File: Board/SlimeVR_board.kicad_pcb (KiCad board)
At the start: 2 copper layers, 55.8 x 44.5 mm, 44 parts, among them IC1 HT7833, J1 USB_C_Receptacle_USB2.0_16P, J2 Conn_01x02_Pin, J3 Conn_01x04_Pin, J5 Conn_01x01_Pin, J6 Conn_01x01_Pin, J7 Conn_01x04_Pin, Q1 DMP3099L, SW1 SW_SPDT, U1 TP4056-42-ESOP8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

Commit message: New Version
skiped few version that ware bad or not good or not funcioning
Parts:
- removed 3V3, 5V, BAT: TestPoint_Pad_1.5x1.5mm, TestPoint:TestPoint_Pad_1.5x1.5mm
- removed the GND at (82.3, 34.4)
- removed the GND at (47.3, 36.0)
- removed the GND at (43.0, 58.9)
- removed REF** (x2): TestPoint_Pad_D1.0mm, TestPoint:TestPoint_Pad_D1.0mm
- added +3.3V: TestPoint_Pad_1.0x1.0mm, TestPoint:TestPoint_Pad_1.0x1.0mm, F.Cu at (66.6, 39.0)
- added +5V: TestPoint_Pad_1.0x1.0mm, TestPoint:TestPoint_Pad_1.0x1.0mm, F.Cu at (44.0, 40.2)
- added BAT+: TestPoint_Pad_1.0x1.0mm, TestPoint:TestPoint_Pad_1.0x1.0mm, F.Cu at (42.0, 55.2)
- added BMI160 #2 GND: TestPoint_Pad_1.5x1.5mm, TestPoint:TestPoint_Pad_1.5x1.5mm, F.Cu at (48.6, 52.2)
- added GND: TestPoint_Pad_1.0x1.0mm, TestPoint:TestPoint_Pad_1.0x1.0mm, F.Cu at (39.9, 55.2)
- added GND: TestPoint_Pad_1.0x1.0mm, TestPoint:TestPoint_Pad_1.0x1.0mm, F.Cu at (73.8, 27.1)
- D1: value LED -> FYLS-1206URC
- D2: value LED -> FYLS-1206PGC
- D3: value LED -> FYLS-1206UWC
- D4: value D -> 1N4148WSQ-7-F
- J2: value Conn_01x02_Pin -> JST-PH
- J3: value Conn_01x04_Pin -> SMD_Pads; footprint Connector_PinSocket_2.54mm:PinSocket_1x04_P2.54mm_Vertical -> Custom:Pin_1x04_SMD_P2.54mm
- J7: value Conn_01x04_Pin -> JTX-HX
- Q1: value DMP3099L -> DMP3099L-7
- R1: value 10k -> 47k
- R2: value 3k3 -> 47k
- SW1: value SW_SPDT -> LA215009; footprint Button_Switch_THT:SW_Slide_SPDT_Angled_CK_OS102011MA1Q -> Button_Switch_THT:SW_Slide-03_Wuerth-WS-SLTV_10x2.5x6.4_P2.54mm
- moved SW1 36.3 mm to (39.0, 30.8)
- moved D3 29.5 mm to (62.0, 31.0)
- moved R8 24.6 mm to (61.5, 34.5)
- moved D4 24.3 mm to (41.0, 33.2), turned to 0 degrees
- moved R1 20.2 mm to (74.3, 63.5), turned to 0 degrees
- moved R2 17.0 mm to (74.3, 61.5)
- moved C8 16.5 mm to (41.9, 38.5)
- moved C1 15.3 mm to (41.9, 37.0)
- moved C4 12.2 mm to (66.1, 36.2)
- moved C7 11.8 mm to (69.6, 36.2)
- moved J2 11.1 mm to (48.9, 59.6)
- moved R10 10.9 mm to (73.5, 30.2)
- moved J6 10.4 mm to (77.0, 30.2)
- moved IC1 9.91 mm to (68.2, 32.8)
- moved R5 9.58 mm to (45.5, 36.2), turned to -90 degrees
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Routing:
- net Net-(D4-K): track 82.0 -> 21.7 mm
- net +5V: track 117.3 -> 62.9 mm
- net Net-(SW1-B): track 22.6 -> 74.0 mm, vias 0 -> 2
- net +3.3V: track 103.9 -> 80.0 mm
- net Net-(J5-Pin_1): track 34.1 -> 12.8 mm, vias 0 -> 2
- net Net-(U2-IO3): track 22.4 -> 4.09 mm, vias 2 -> 0
- net Net-(J3-Pin_3): track 68.0 -> 50.2 mm, vias 1 -> 0
- net Net-(J3-Pin_4): track 66.1 -> 49.6 mm, vias 1 -> 0
- net D-: track 29.4 -> 42.0 mm
- net Earth: track 12.2 -> 0.00 mm, vias 23 -> 117
- net D+: track 32.1 -> 43.6 mm
- net Net-(U1-~{CHRG}): track 19.0 -> 7.53 mm
- net Net-(D3-A): track 25.6 -> 17.2 mm
- net +BATT: track 33.9 -> 26.3 mm
- net Net-(U1-~{STDBY}): track 17.0 -> 9.92 mm
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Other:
- board size 55.8 x 44.5 mm -> 51.8 x 39.5 mm
- board text added: "*Note: for BMI160 bridge bouth GNDs as show in SlimeVR Documentation*"
- board text added: "+3V3"
- board text added: "- +"
- board text added: "GND"
- board text added: "ICM-4586 LSM6DSV LSM6DSR BMI160 *Note*"
- board text added: "None"
- board text added: "Powered \/ \/"
- board text added: "SCl"
- board text added: "SDA"
- board text added: "Switch is angled 90°"
- board text added: "Ver.: 0.9C"
- board text removed: "ICM-4586 LSM6DSV LSM6DSR BMI160 *Note the BMI160 module requires 2 Ground conections*"

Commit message: New version
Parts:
- removed +3.3V, +5V, BAT+: TestPoint_Pad_1.0x1.0mm, TestPoint:TestPoint_Pad_1.0x1.0mm
- removed the GND at (39.9, 55.2)
- removed the GND at (73.8, 27.1)
- added 3V3: TestPoint_Pad_1.0x1.0mm, TestPoint:TestPoint_Pad_1.0x1.0mm, F.Cu at (53.4, 26.4)
- added 3V3: TestPoint_Pad_1.0x1.0mm, TestPoint:TestPoint_Pad_1.0x1.0mm, F.Cu at (59.1, 35.4)
- added 5V: TestPoint_Pad_1.0x1.0mm, TestPoint:TestPoint_Pad_1.0x1.0mm, F.Cu at (78.8, 31.3)
- added BAT: TestPoint_Pad_1.0x1.0mm, TestPoint:TestPoint_Pad_1.0x1.0mm, F.Cu at (95.2, 43.3)
- added BMI160 #2 GND: TestPoint_Pad_1.5x1.5mm, TestPoint:TestPoint_Pad_1.5x1.5mm, F.Cu at (53.2, 44.6)
- added GND: TestPoint_Pad_1.0x1.0mm, TestPoint:TestPoint_Pad_1.0x1.0mm, F.Cu at (37.6, 26.4)
- added GND: TestPoint_Pad_1.0x1.0mm, TestPoint:TestPoint_Pad_1.0x1.0mm, F.Cu at (70.5, 31.4)
- added J4: SMD_Pads, Custom:Pin_1x04_SMD_P2.54mm, F.Cu at (45.0, 46.4)
- added J8: JTX-HX-A-1, Connector_JST:JST_XH_S4B-XH-A-1_1x04_P2.50mm_Horizontal, F.Cu at (49.3, 25.4)
- J7: value JTX-HX -> JTX-HX-A-1; footprint Connector_JST:JST_XH_S4B-XH-A_1x04_P2.50mm_Horizontal -> Connector_JST:JST_XH_S4B-XH-A-1_1x04_P2.50mm_Horizontal
- U1: value TP4056-42-ESOP8 -> TP4056-ESOP8
- U2: value ESP32-C3-WROOM-02 -> ESP32-C3-WROOM-02-N4
- moved SW1 52.4 mm to (91.0, 24.5)
- moved C8 50.5 mm to (92.2, 34.1)
- moved C1 50.5 mm to (92.2, 32.6)
- moved R7 50.5 mm to (89.5, 36.0)
- moved U1 50.5 mm to (91.5, 39.7)
- moved R11 49.7 mm to (90.5, 30.9), turned to 0 degrees
- moved D4 49.6 mm to (90.4, 28.8)
- moved Q1 48.5 mm to (88.3, 44.0), turned to 0 degrees
- moved J2 45.0 mm to (92.0, 46.5), turned to 0 degrees
- moved D1 36.9 mm to (82.0, 25.9)
- moved D2 36.9 mm to (84.5, 25.9)
- moved R5 36.9 mm to (82.0, 30.4)
- moved R6 36.9 mm to (84.5, 30.4)
- moved BMI160 #2 GND 36.1 mm to (84.4, 48.0), turned to 90 degrees
- moved J7 31.2 mm to (84.6, 64.2)
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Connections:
- net Net-(J3-Pin_4) renamed SDA
- net Net-(U2-IO3) renamed Battery_sence
- J3 pad 3: Net-(J3-Pin_3) -> SCL
- J7 pad 2: Earth -> SCL
- J7 pad 3: Net-(J3-Pin_3) -> Earth
- U2 pad 4: Net-(J3-Pin_3) -> SCL
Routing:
- net SCL: track 0.00 -> 63.6 mm
- net Net-(J3-Pin_3): track 50.2 -> 0.00 mm
- net Net-(J5-Pin_1): track 12.8 -> 45.1 mm
- net +3.3V: track 80.0 -> 109.9 mm, vias 0 -> 5
- net SDA: track 49.6 -> 74.7 mm
- net Net-(D3-A): track 17.2 -> 36.8 mm
- net +BATT: track 26.3 -> 12.5 mm
- net Net-(U1-~{CHRG}): track 7.53 -> 21.1 mm, vias 0 -> 2
- net Net-(J6-Pin_1): track 19.1 -> 31.9 mm
- net +5V: track 62.9 -> 75.6 mm, vias 0 -> 2
- net Battery_sence: track 4.09 -> 15.0 mm
- net Net-(U1-~{STDBY}): track 9.92 -> 20.5 mm, vias 0 -> 2
- net Net-(SW1-B): track 74.0 -> 70.2 mm
- net D+: track 43.6 -> 40.2 mm, vias 2 -> 0
- net Net-(D4-K): track 21.7 -> 24.4 mm
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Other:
- board size 51.8 x 39.5 mm -> 61 x 50 mm
- board text added: "Ver.: 2.5W"
- board text added: "Ver.: 2.5WE"
- board text added: "©2025 Skaut0071"
- board text removed: "Ver.: 0.9C"

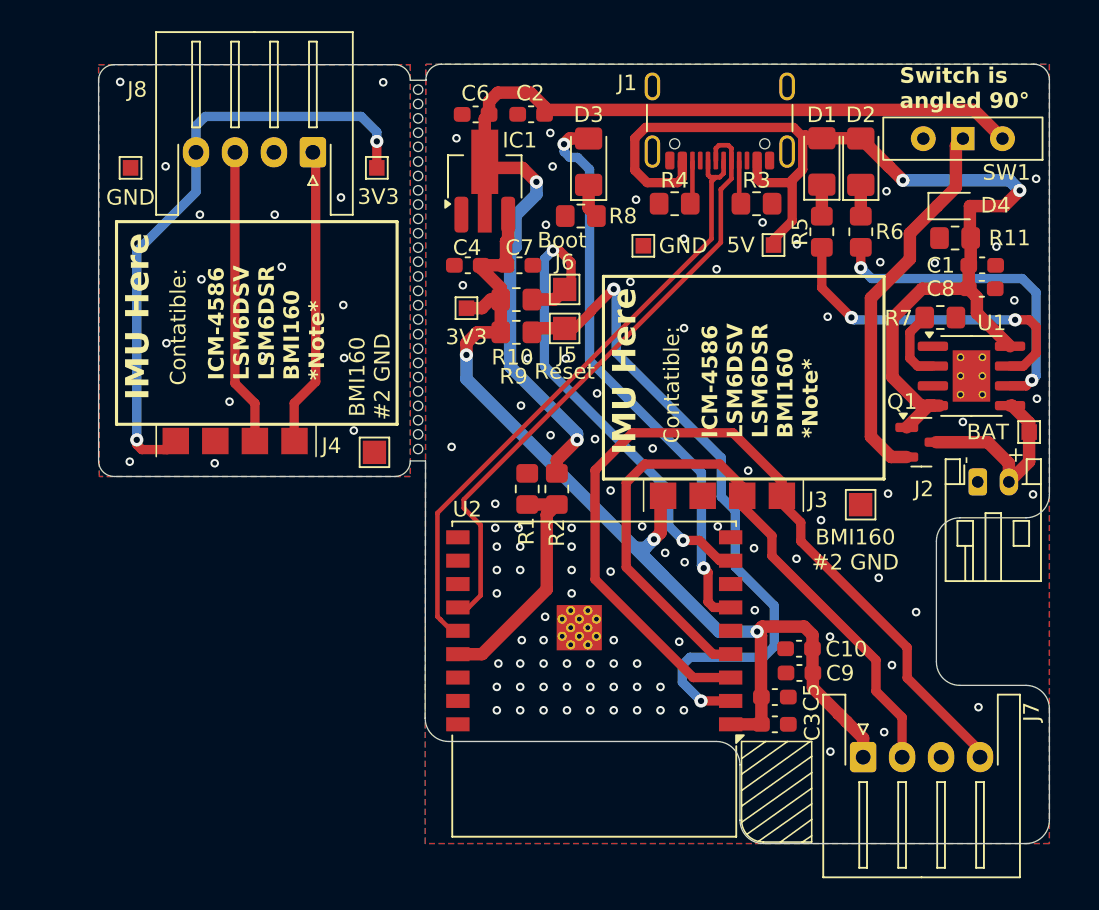
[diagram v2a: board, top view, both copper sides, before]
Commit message: New version of board
Fixex:
- grafical issues and speling
- wrong diode used, board wont get more then 150mA
- battery pins has been swaped for standarizes conection
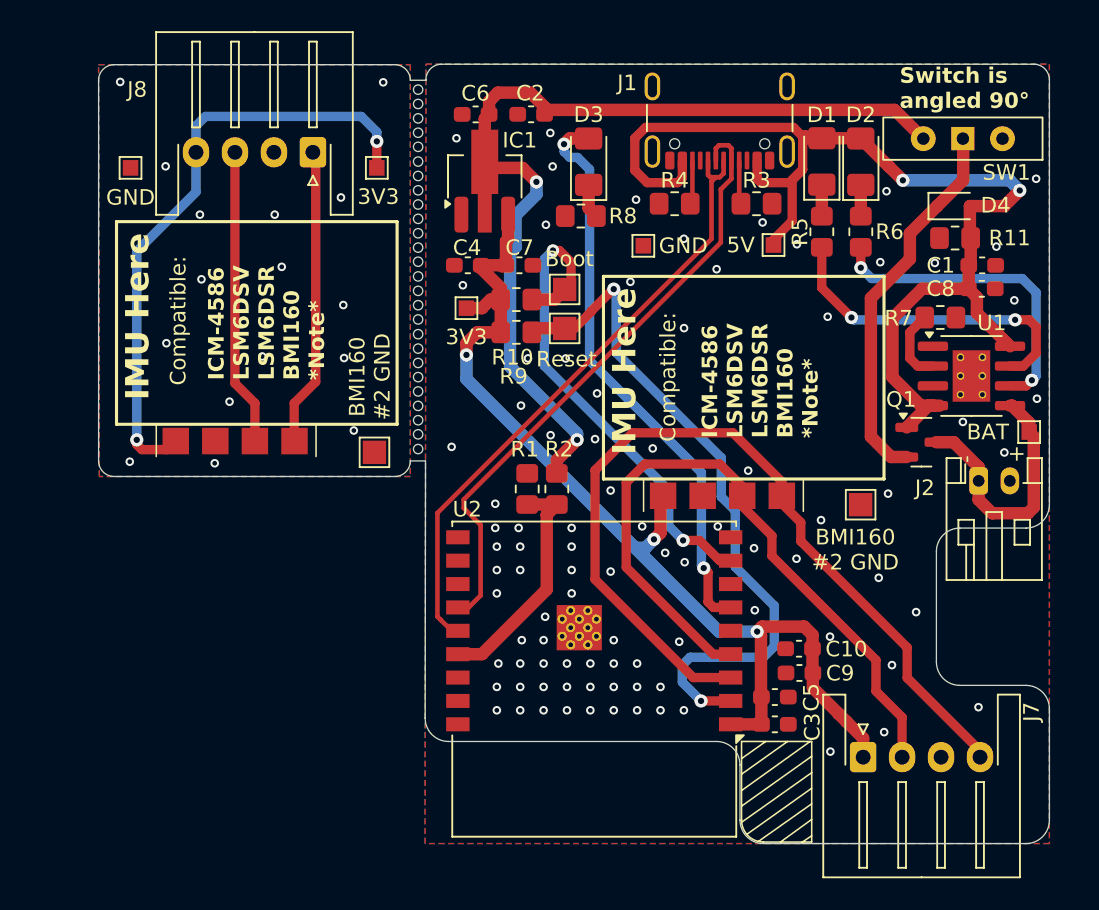
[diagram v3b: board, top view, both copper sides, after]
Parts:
- C3: value 1uF -> 47uF
- C7: value 1uF -> 10uF
- D4: value 1N4148WSQ-7-F -> 1N4448WSF-7
- moved J2 0.09 mm to (92.0, 46.4)
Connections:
- C2 pad 1: Net-(SW1-B) -> Net-(SW1-C)
- C6 pad 1: Net-(SW1-B) -> Net-(SW1-C)
- IC1 pad 2: Net-(SW1-B) -> Net-(SW1-C)
- J2 pad 1: Earth -> +BATT
- J2 pad 2: +BATT -> Earth
- R2 pad 1: Net-(SW1-B) -> Net-(SW1-C)
- SW1 pad 2: Net-(SW1-B) -> unconnected-(SW1-B-Pad2)
- SW1 pad 3: unconnected-(SW1-C-Pad3) -> Net-(SW1-C)
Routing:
- net Net-(SW1-B): track 70.2 -> 0.00 mm, vias 2 -> 0
- net Net-(SW1-C): track 0.00 -> 65.1 mm, vias 0 -> 2
- net +BATT: track 12.5 -> 16.8 mm
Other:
- outline, holes or cut-outs redrawn
- board text added: "Compatible:"
- board text added: "SlimeVR Board of ESP32C3 WROOM and BMI160 compatible IMUs"
- board text added: "Ver.: 2.6W"
- board text added: "Ver.: 2.6WE"
- board text removed: "Contatible:"
- board text removed: "SlimeVR Board of ESP32C3 WROOM and BMI160 contatible IMUs"
- board text removed: "Ver.: 2.5W"
- board text removed: "Ver.: 2.5WE"
